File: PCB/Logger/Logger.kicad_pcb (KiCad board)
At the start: 2 copper layers, 70 x 70 mm, 74 parts, among them J1 JST-PH-SM4-TB, J2 USB-C-Socket-V, J3 Conn_01x05, J4 Shelly, J5 USB-PROG, J6 TF_PUSH, Q1 CJ2301, Q2 C179347, U1 ESP32-S3-MINI-1, U3 TP4054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

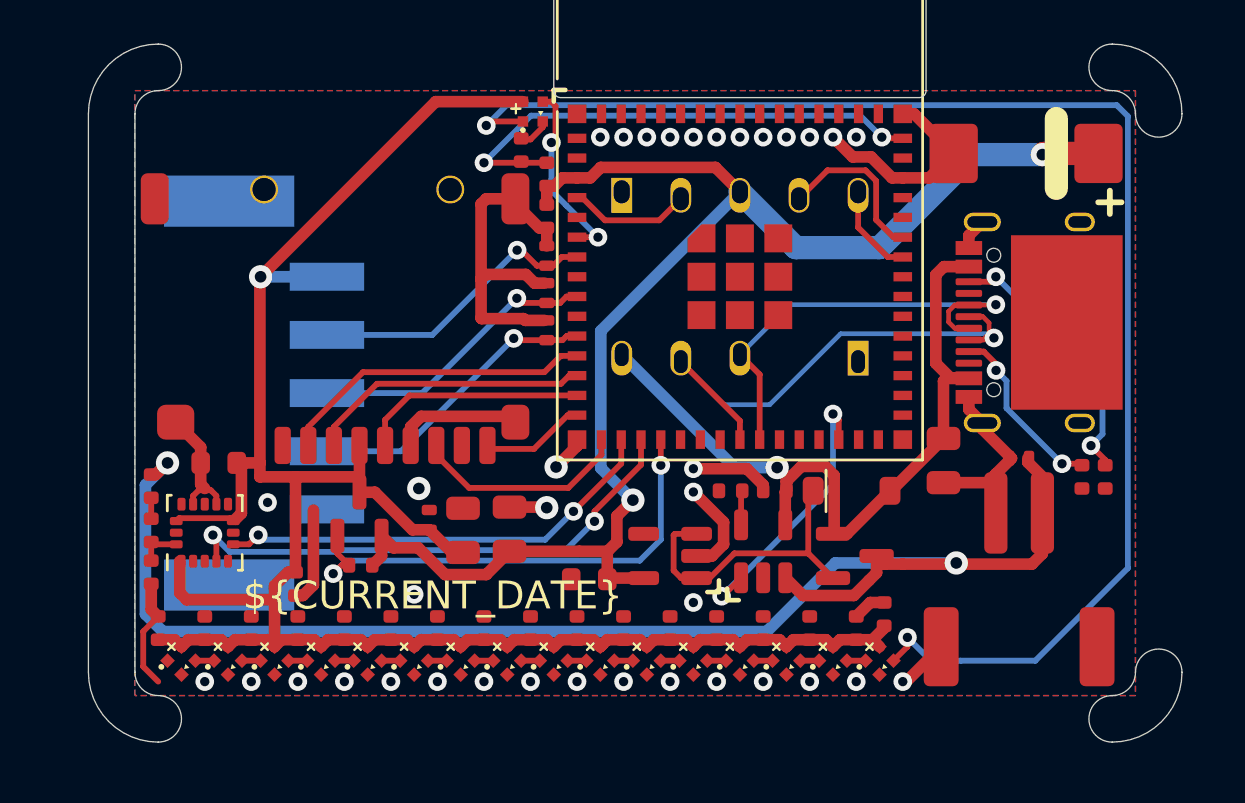
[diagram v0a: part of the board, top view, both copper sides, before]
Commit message: Move charger input
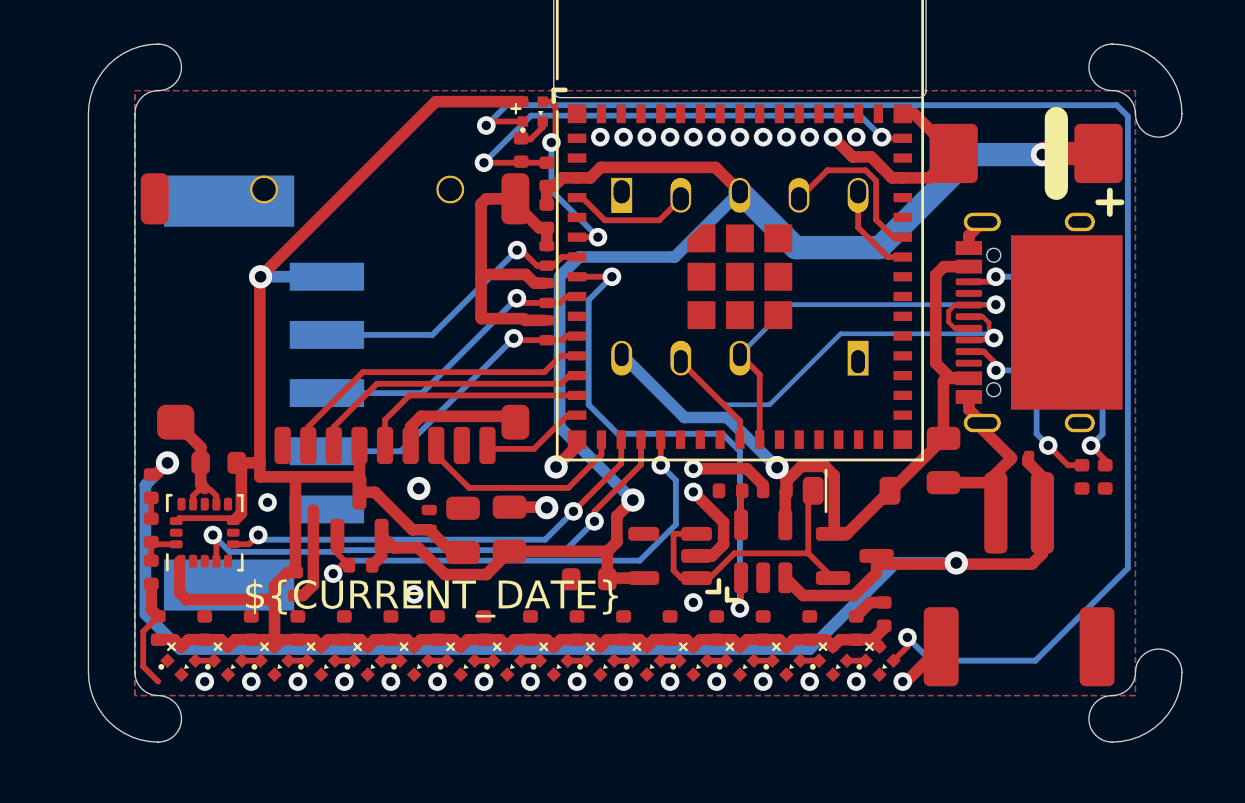
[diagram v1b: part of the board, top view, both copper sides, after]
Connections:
- U1 pad 28: STAT -> unconnected-(U1-GPIO33-Pad28)
- U1 pad 8: unconnected-(U1-GPIO4-Pad8) -> CHARGER
- U3 pad 1: STAT -> CHARGER
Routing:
- net CHARGER: track 0.00 -> 22.8 mm, vias 0 -> 2
- net STAT: track 12.2 -> 0.00 mm, vias 2 -> 0
- net +3.3V: track 61.9 -> 65.7 mm
- net Net-(J2-CC2): track 11.7 -> 13.3 mm
- net Net-(J2-CC1): track 7.74 -> 8.37 mm
- net VBAT: track 59.8 -> 60.4 mm
- net GND: track 69.9 -> 69.3 mm
- net PWR: track 21.3 -> 21.8 mm
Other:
- board text added: "2 3 4 5 7 8 9 10 11 12 13 14 15"
- board text added: "RGB GPSTICK CHARGER GPSRX GPSTX SDSS SDMOSI SDSCK SDCD SDMISO ACCSDA ACCSCL PWR"
- board text removed: "2 3 5 7 8 9 10 11 12 13 14 15 33"
- board text removed: "RGB GPSTICK GPSRX GPSTX SDSS SDMOSI SDSCK SDCD SDMISO ACCSDA ACCSCL PWR STAT"

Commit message: Tweak
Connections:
- net ADC renamed ADC1

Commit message: Rework
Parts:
- added R10: 1R 1W, RevK:R_1218, F.Cu at (94.2, 109.5)
- moved C18 5.71 mm to (86.4, 108.4), turned to -90 degrees
- moved C1 4.18 mm to (98.0, 110.2), turned to -90 degrees
- moved C20 3.44 mm to (98.8, 107.8), turned to 0 degrees
- moved D6 2.85 mm to (87.8, 108.4), turned to 90 degrees
- moved Q2 2.55 mm to (90.0, 109.1)
- moved R6 2.51 mm to (90.0, 111.4)
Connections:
- Q2 pad 2: +3.3V -> Net-(Q2-S)
- R6 pad 1: +3.3V -> Net-(Q2-S)
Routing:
- net GND: track 69.3 -> 86.5 mm, vias 36 -> 35
- net +3.3V: track 65.7 -> 55.6 mm
- net Net-(Q2-S): track 0.00 -> 5.26 mm
- net PWR: track 21.8 -> 17.1 mm
- net SPWR: track 92.6 -> 90.9 mm
- net ACCSDA: track 19.3 -> 20.3 mm
- net CHARGER: track 22.8 -> 22.2 mm
- net D-: track 23.5 -> 22.9 mm
- net ACCSCL: track 22.8 -> 23.3 mm

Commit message: EAN
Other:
- board text added: "5060634238182"

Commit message: Tidy
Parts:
- added Q3: CJ2301, RevK:SOT-23, F.Cu at (108.0, 110.4)
- added R11: 100K 1%, RevK:R_0402, F.Cu at (112.5, 97.0)
- moved Q1 2.48 mm to (108.0, 107.7), turned to 90 degrees
- moved D2 1.90 mm to (110.5, 108.2), turned to 90 degrees
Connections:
- net CHARGER renamed CHARGING
- U1 pad 10: unconnected-(U1-GPIO6-Pad10) -> USB
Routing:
- net +3.3V: track 55.6 -> 87.3 mm, vias 2 -> 3
- net USB: track 0.00 -> 27.5 mm, vias 0 -> 2
- net Net-(D2-K): track 12.9 -> 20.9 mm, vias 0 -> 2
- net GND: track 86.5 -> 94.2 mm, vias 35 -> 36
- net VBAT: track 60.4 -> 65.3 mm, vias 2 -> 4
- net VBUS: track 34.0 -> 37.4 mm, vias 1 -> 2
- net ACCSDA: track 20.3 -> 22.4 mm
- net CHARGING: track 22.2 -> 20.2 mm
- net ACCSCL: track 23.3 -> 25.0 mm
- net PWR: track 17.1 -> 18.5 mm
- net Net-(J2-CC2): track 13.3 -> 12.3 mm
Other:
- board text added: "2 3 4 5 6 7 8 9 10 11 12 13 14 15"
- board text added: "RGB GPSTICK CHARGING GPSRX USB GPSTX SDSS SDMOSI SDSCK SDCD SDMISO ACCSDA ACCSCL PWR"
- board text removed: "2 3 4 5 7 8 9 10 11 12 13 14 15"
- board text removed: "RGB GPSTICK CHARGER GPSRX GPSTX SDSS SDMOSI SDSCK SDCD SDMISO ACCSDA ACCSCL PWR"
